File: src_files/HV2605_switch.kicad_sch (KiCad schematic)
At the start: 16 parts

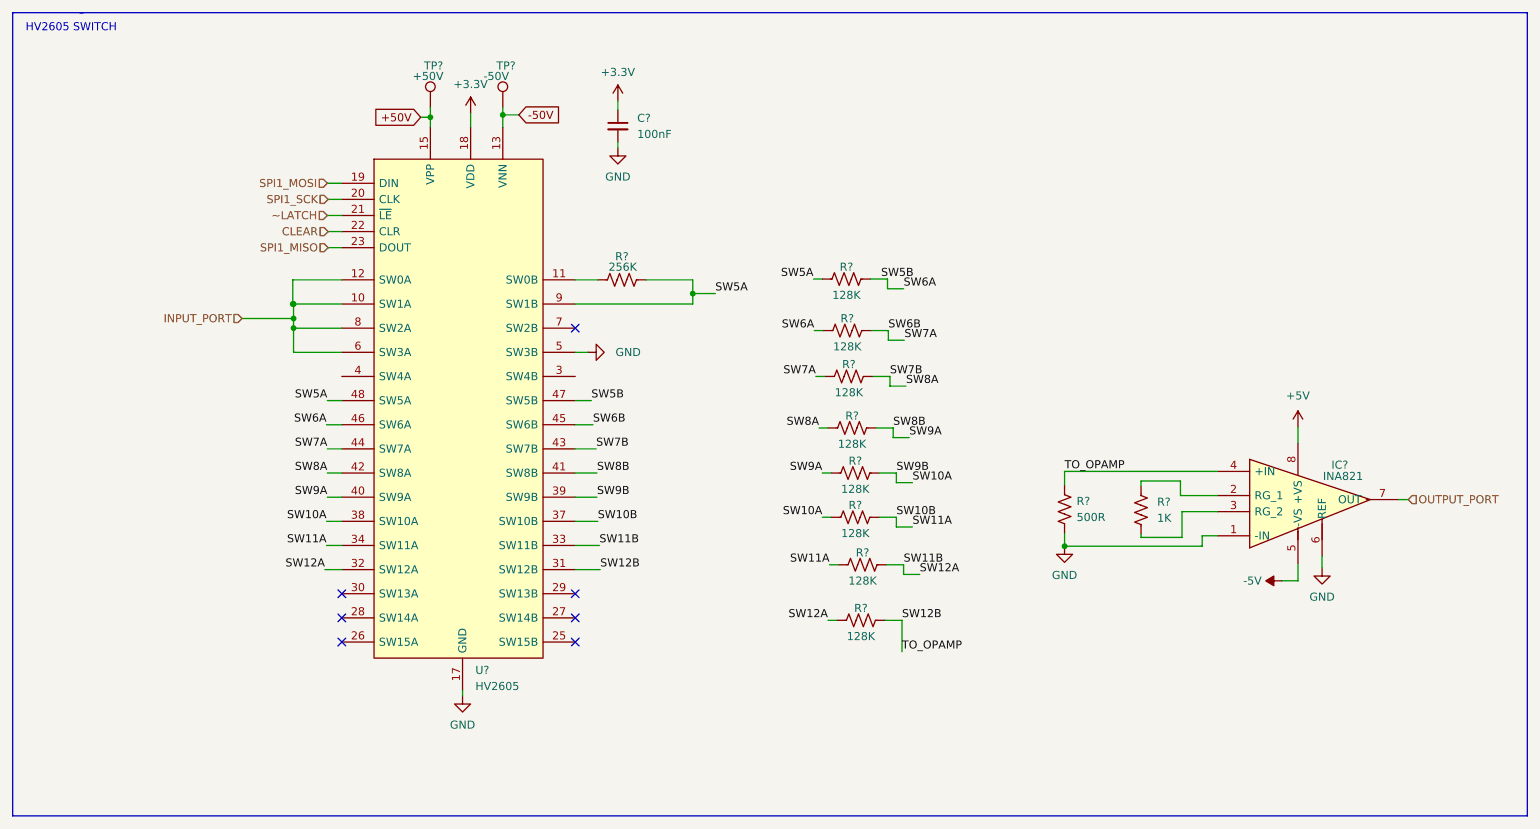
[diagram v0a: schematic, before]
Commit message: updated footprint assignment
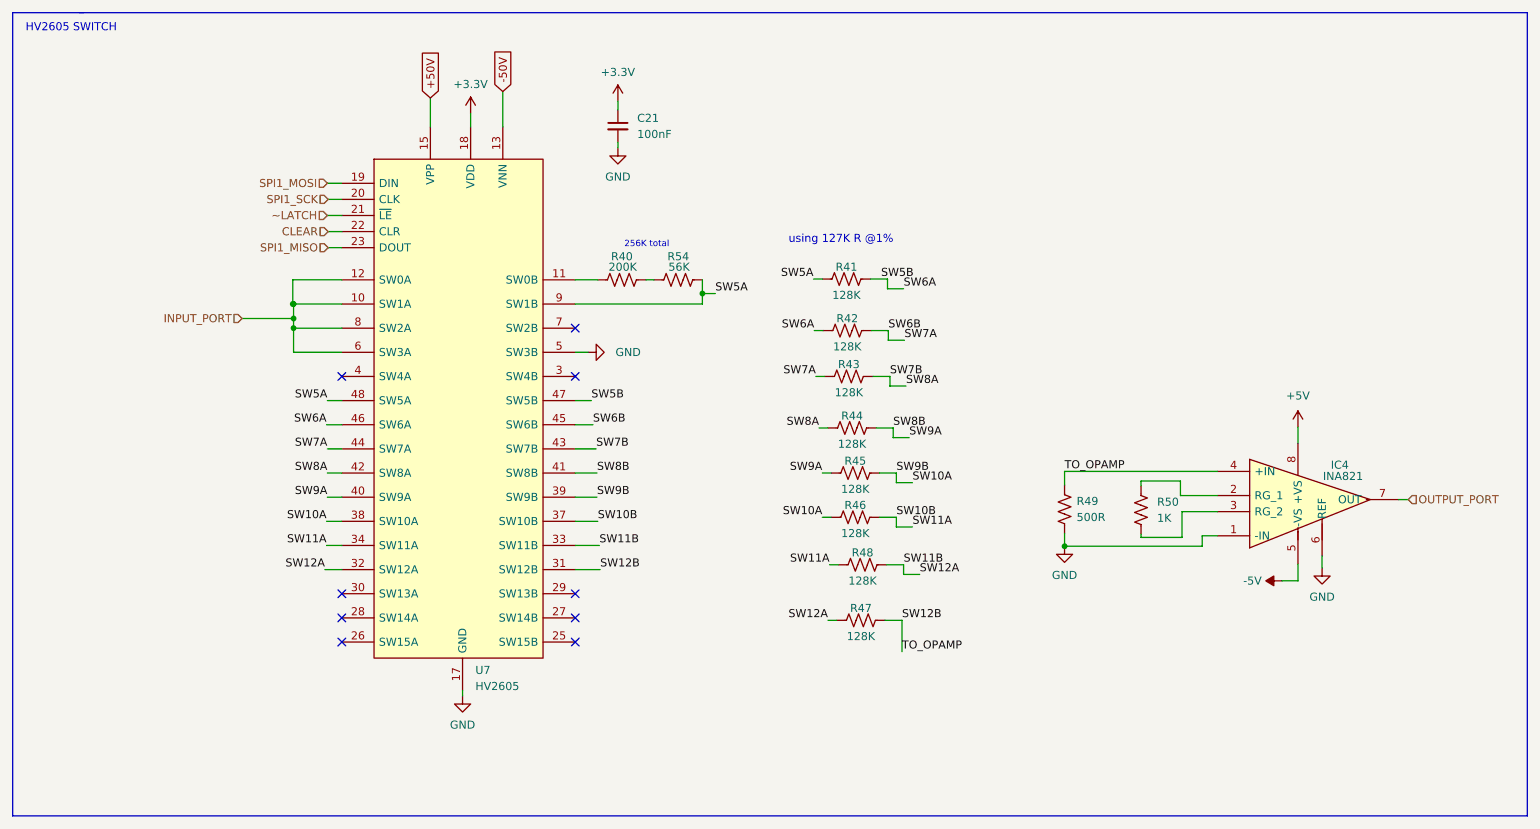
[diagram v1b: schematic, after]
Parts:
- removed TP?: +50V, symbol Connector:TestPoint
- removed TP?: -50V, symbol Connector:TestPoint
- added R54: 56K, Resistor_SMD:R_0603_1608Metric_Pad0.98x0.95mm_HandSolder, symbol Device:R_US
- C21: renamed from C?; footprint (none) -> Capacitor_SMD:C_0603_1608Metric_Pad1.08x0.95mm_HandSolder
- IC4: renamed from IC?; footprint SOP65P490X110-8N -> Capacitor_SMD:C_0603_1608Metric_Pad1.08x0.95mm_HandSolder
- R40: renamed from R?; value 256K -> 200K; footprint (none) -> Resistor_SMD:R_0603_1608Metric_Pad0.98x0.95mm_HandSolder
- R41, R42, R43, R44, R45, R46, R47, R48, R50: renamed from R?; footprint (none) -> Resistor_SMD:R_0603_1608Metric_Pad0.98x0.95mm_HandSolder
- R49: renamed from R?; footprint (none) -> Resistor_SMD:R_0805_2012Metric_Pad1.20x1.40mm_HandSolder
- U7: renamed from U?; footprint QFP50P900X900X160-48N -> Package_QFP:TQFP-48_7x7mm_P0.5mm
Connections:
- net SW5A: now also R54.2; no longer R40.2
- new net: R40.2, R54.1
- no-connect marks 7 -> 9
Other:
- note added: "256K total"
- note added: "using 127K R @1%"
